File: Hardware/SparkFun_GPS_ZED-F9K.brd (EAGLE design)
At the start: 43.2 x 43.2 mm, 47 parts, among them J1 QWIIC_RIGHT_ANGLE, J4 U.FL, J6 QWIIC_RIGHT_ANGLE, U1 UBLOX_ZED_F9K, U2 3.3V, U3 TRIPLE_BUFFER_74LVC3G07

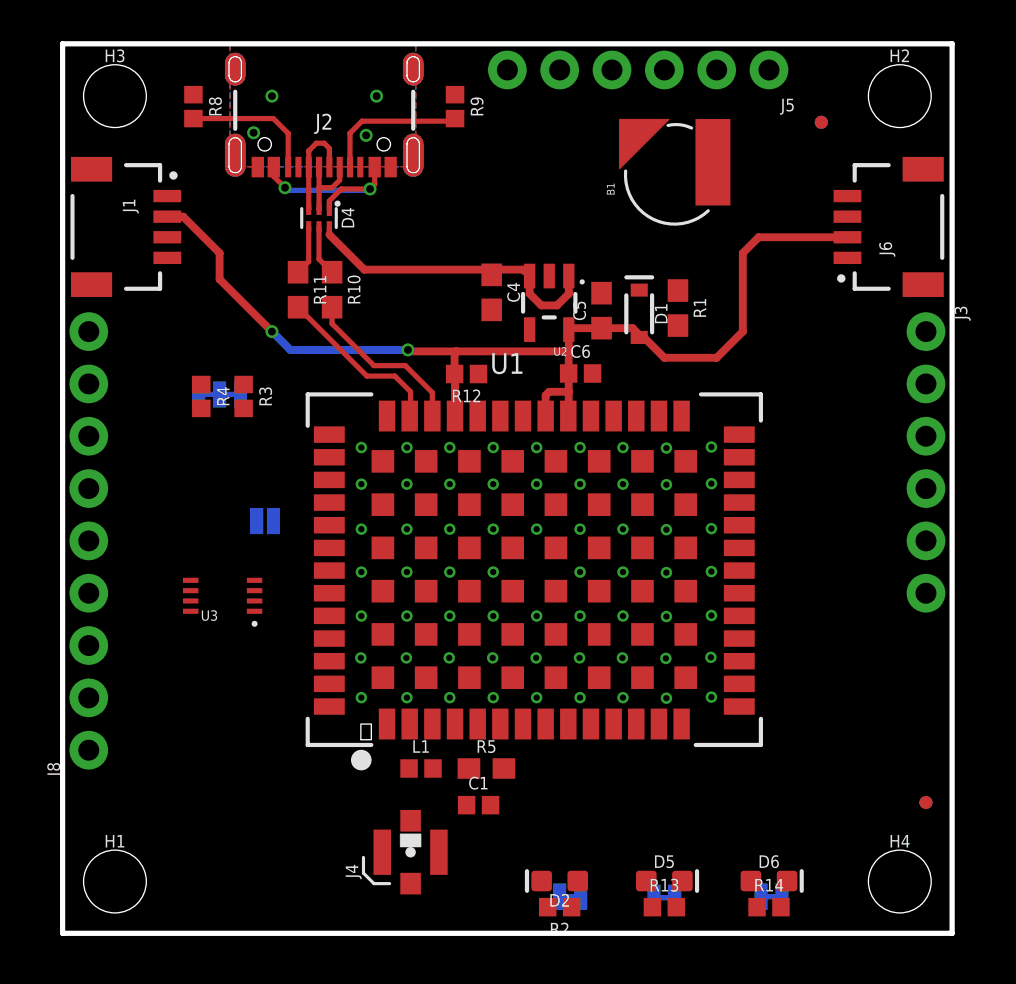
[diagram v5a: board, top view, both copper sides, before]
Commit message: Finalizes trace work for the Breakout board
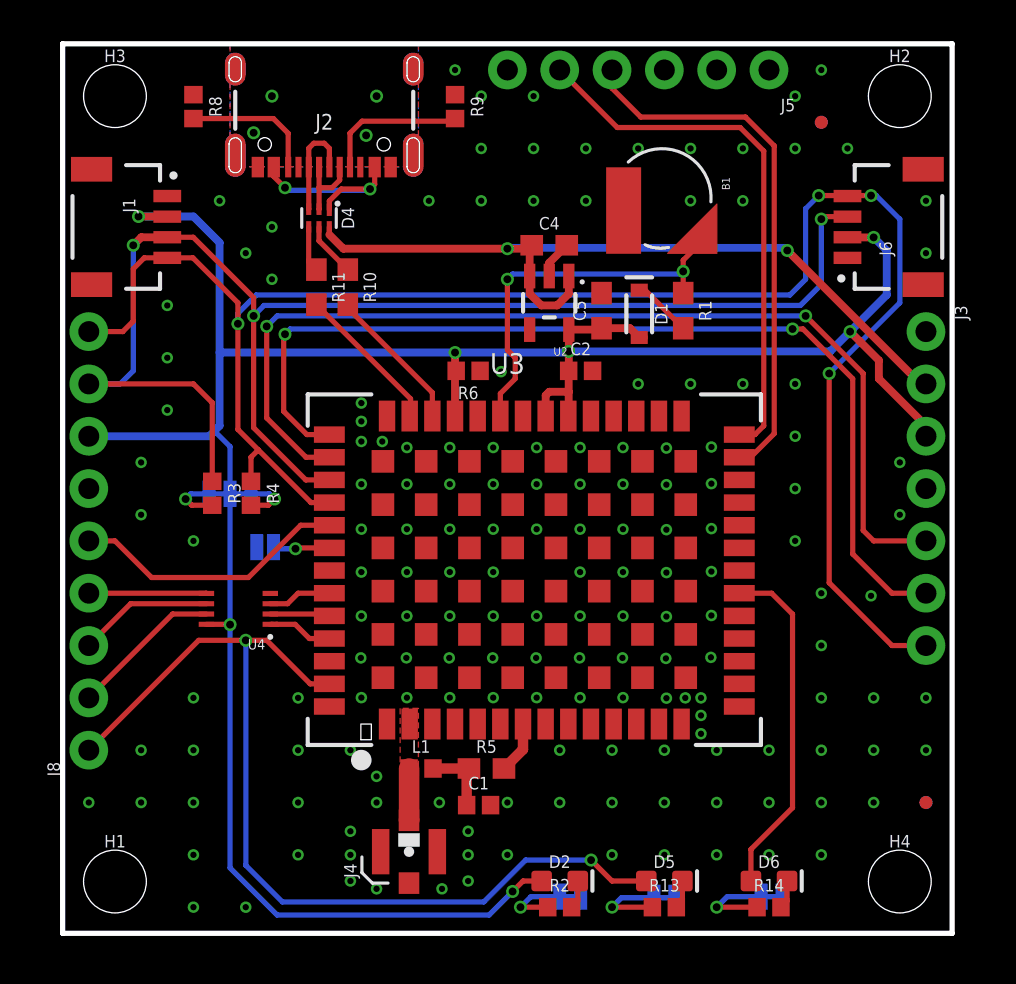
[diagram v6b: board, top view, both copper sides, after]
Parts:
- removed C6: 1.0uF, SparkFun-Capacitors:0402
- removed R12: 100K, SparkFun-Resistors:0402
- removed U1: UBLOX_ZED_F9K, classified:UBLOX_ZED_F9K
- added C2: 1.0uF, SparkFun-Capacitors:0402
- added R6: 100K, SparkFun-Resistors:0402
- added U4: TRIPLE_BUFFER_74LVC3G07, classified:SOP_8-PIN
- J3: device SparkFun-Connectors:1X06_NO_SILK -> SparkFun-Connectors:1X07_NO_SILK
- U3: value TRIPLE_BUFFER_74LVC3G07 -> UBLOX_ZED_F9K; device classified:SOP_8-PIN -> classified:UBLOX_ZED_F9K
- moved U3 15.2 mm to (22.9, 17.8), turned to 0 degrees
- moved R4 5.28 mm to (9.14, 21.4)
- moved R3 4.94 mm to (7.26, 21.4)
- moved JP2 4.85 mm to (8.13, 21.3), turned to 180 degrees
- moved C4 3.61 mm to (23.6, 33.4), turned to 0 degrees
- moved B1 1.31 mm to (29.1, 35.7), turned to 270 degrees
- moved JP1 1.27 mm to (9.83, 18.7)
- moved R11 0.90 mm to (12.3, 31.4)
- moved R10 0.77 mm to (13.8, 31.4)
- moved R1 0.28 mm to (30.1, 30.2)
- moved J4 0.08 mm to (16.8, 3.96)
- turned D2 to 0 degrees
- turned PWR to 0 degrees
- turned R2 to 0 degrees
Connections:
- removed net DIR: U1.P23
- removed net SCK: J3.6
- removed net WT: U1.P22
- net !CS: now also J3.4; no longer J3.3
- net !RESET_IN: now also U3.P49, U4.P3; no longer U1.P49, U3.P1
- net !RESET_OUT: now also U4.P7; no longer U3.P7
- net !SAFEBOOT_IN: now also U4.P6; no longer U1.P50, U3.P6
- net !SAFEBOOT_OUT: now also U3.P50, U4.P2; no longer U3.P2
- net 3.3V: now also C2.1, J3.3, R6.2, U3.P33, U3.P34, U3.P38, U4.P8; no longer C6.1, R12.2, U1.P33, U1.P34, U1.P38, U3.P8
- net DMINUS: now also U3.P39; no longer U1.P39
- net DPLUS: now also U3.P40; no longer U1.P40
- net D_SEL: now also U3.P47; no longer U1.P47
- net GND: now also C2.2, R6.1, U3.G1, U3.G10, U3.G11, U3.G12, U3.G13, U3.G14, U3.G15, U3.G16, U3.G17, U3.G18, U3.G19, U3.G2, U3.G20, U3.G21, U3.G22, U3.G23, U3.G24, U3.G25, U3.G26, U3.G27, U3.G28, U3.G29, U3.G3, U3.G30, U3.G31, U3.G32, U3.G33, U3.G34, U3.G35, U3.G36, U3.G37, U3.G38, U3.G39, U3.G4, U3.G40, U3.G41, U3.G42, U3.G43, U3.G44, U3.G45, U3.G46, U3.G47, U3.G48, U3.G5, U3.G6, U3.G7, U3.G8, U3.G9, U3.P1, U3.P12, U3.P14, U3.P3, U3.P32, U3.P37, U3.P41, U3.P48, U4.P4; no longer C6.2, R12.1, U1.G1, U1.G10, U1.G11, U1.G12, U1.G13, U1.G14, U1.G15, U1.G16, U1.G17, U1.G18, U1.G19, U1.G2, U1.G20, U1.G21, U1.G22, U1.G23, U1.G24, U1.G25, U1.G26, U1.G27, U1.G28, U1.G29, U1.G3, U1.G30, U1.G31, U1.G32, U1.G33, U1.G34, U1.G35, U1.G36, U1.G37, U1.G38, U1.G39, U1.G4, U1.G40, U1.G41, U1.G42, U1.G43, U1.G44, U1.G45, U1.G46, U1.G47, U1.G48, U1.G5, U1.G6, U1.G7, U1.G8, U1.G9, U1.P1, U1.P12, U1.P14, U1.P3, U1.P32, U1.P37, U1.P41, U1.P48, U3.P4
- net INT_IN: now also U3.P51, U4.P1; no longer U1.P51, U3.P3
- net INT_OUT: now also U4.P5; no longer U3.P5
- net PPS: now also U3.P53; no longer U1.P53
- net RF_IN: now also U3.P2; no longer U1.P2
- net RTK_STAT: now also U3.P20; no longer U1.P20
- net RXI/MOSI: now also J3.5, U3.P43; no longer J3.4, U1.P43
- net RXI2: now also U3.P26; no longer U1.P26
- net SCL/CLK: now also J3.7, U3.P45; no longer U1.P45
- net SDA/!CS: now also U3.P44; no longer U1.P44
- net TXO/MISO: now also J3.6, U3.P42; no longer J3.5, U1.P42
- net TXO2: now also U3.P27; no longer U1.P27
- net TX_READY: now also U3.P46; no longer U1.P46
- net V_BATT: now also U3.P36; no longer U1.P36
- net V_RF: now also U3.P7; no longer U1.P7
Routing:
- net SCL/CLK: track 0.00 -> 87.4 mm, vias 0 -> 4
- net SDA/!CS: track 0.00 -> 69.6 mm, vias 0 -> 3
- net 3.3V: track 51.5 -> 119.1 mm, vias 2 -> 7
- net RXI/MOSI: track 0.00 -> 49.5 mm, vias 0 -> 2
- net TXO/MISO: track 0.00 -> 48.0 mm, vias 0 -> 2
- net PPS: track 0.00 -> 47.1 mm, vias 0 -> 2
- net TXO2: track 0.00 -> 26.2 mm
- net RXI2: track 0.00 -> 26.1 mm
- net VIN: track 15.2 -> 39.1 mm, vias 0 -> 2
- net V_BATT: track 0.00 -> 18.8 mm, vias 0 -> 2
- net RTK_STAT: track 0.00 -> 16.8 mm
- net TX_READY: track 0.00 -> 13.5 mm
- net !RESET_OUT: track 0.00 -> 7.40 mm
- net !SAFEBOOT_IN: track 0.00 -> 6.55 mm
- net INT_OUT: track 0.00 -> 5.71 mm
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- added copper zone on layer 1, net RF_IN

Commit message: Adds a few more vias
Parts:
- moved C1 0.25 mm to (20.2, 6.48)
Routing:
- net GND: vias 162 -> 166
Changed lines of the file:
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@@
 <attribute name="REV" value="" x="1.778" y="-16.256" size="1.778" layer="27" font="vector" ratio="15" display="off"/>
 </element>
-<element name="C1" library="SparkFun-Capacitors" package="0402" value="0.1uF" x="20.193" y="6.223" smashed="yes">
-<attribute name="NAME" x="20.193" y="6.985" size="0.6096" layer="25" font="vector" ratio="20" align="bottom-center"/>
-<attribute name="PROD_ID" value="CAP-12416" x="20.193" y="6.223" size="1.778" layer="27" font="vector" ratio="15" display="off"/>
-<attribute name="VALUE" x="20.193" y="5.461" size="0.6096" layer="27" font="vector" ratio="20" align="top-center"/>
+<element name="C1" library="SparkFun-Capacitors" package="0402" value="0.1uF" x="20.193" y="6.477" smashed="yes">
+<attribute name="NAME" x="20.193" y="7.239" size="0.6096" layer="25" font="vector" ratio="20" align="bottom-center"/>
+<attribute name="PROD_ID" value="CAP-12416" x="20.193" y="6.477" size="1.778" layer="27" font="vector" ratio="15" display="off"/>
+<attribute name="VALUE" x="20.193" y="5.715" size="0.6096" layer="27" font="vector" ratio="20" align="top-center"/>
 </element>
 <element name="L1" library="SparkFun-Coils" package="0402" value="3.9NH" x="17.399" y="8.001" smashed="yes">
@@
 <via x="13.97" y="2.54" extent="1-16" drill="0.3048"/>
 <via x="13.97" y="4.953" extent="1-16" drill="0.3048"/>
+<via x="20.32" y="31.75" extent="1-16" drill="0.3048"/>
+<via x="17.78" y="31.75" extent="1-16" drill="0.3048"/>
+<via x="15.24" y="31.75" extent="1-16" drill="0.3048"/>
+<via x="15.24" y="34.29" extent="1-16" drill="0.3048"/>
 </signal>
 <signal name="3.3V">
@@
 <wire x1="19.724" y1="8.001" x2="17.979" y2="8.001" width="0.508" layer="1"/>
 <wire x1="19.724" y1="8.001" x2="19.613" y2="7.89" width="0.508" layer="1"/>
-<wire x1="19.613" y1="7.89" x2="19.613" y2="6.223" width="0.508" layer="1"/>
+<wire x1="19.613" y1="7.89" x2="19.613" y2="6.477" width="0.508" layer="1"/>
 </signal>
 <signal name="V_RF">

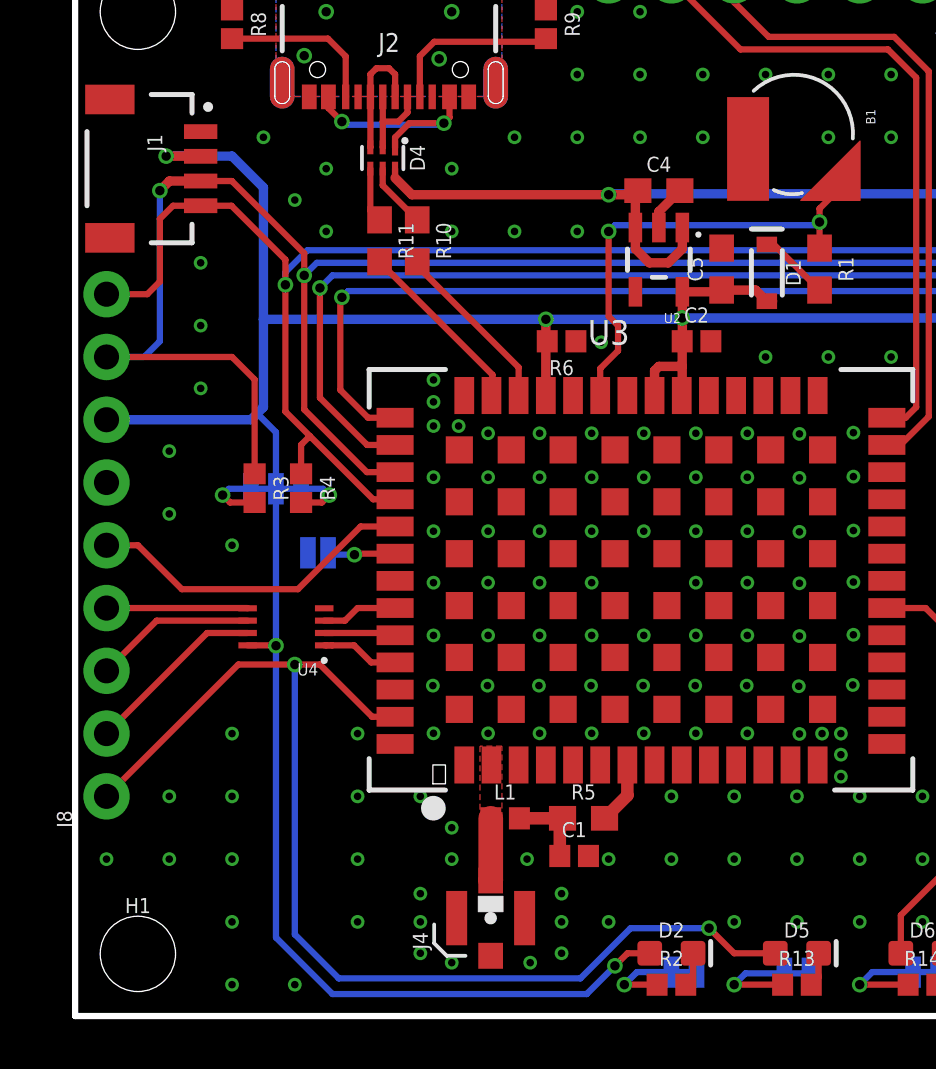
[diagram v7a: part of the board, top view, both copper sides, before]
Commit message: Updates Modules, adjusts ground pour.
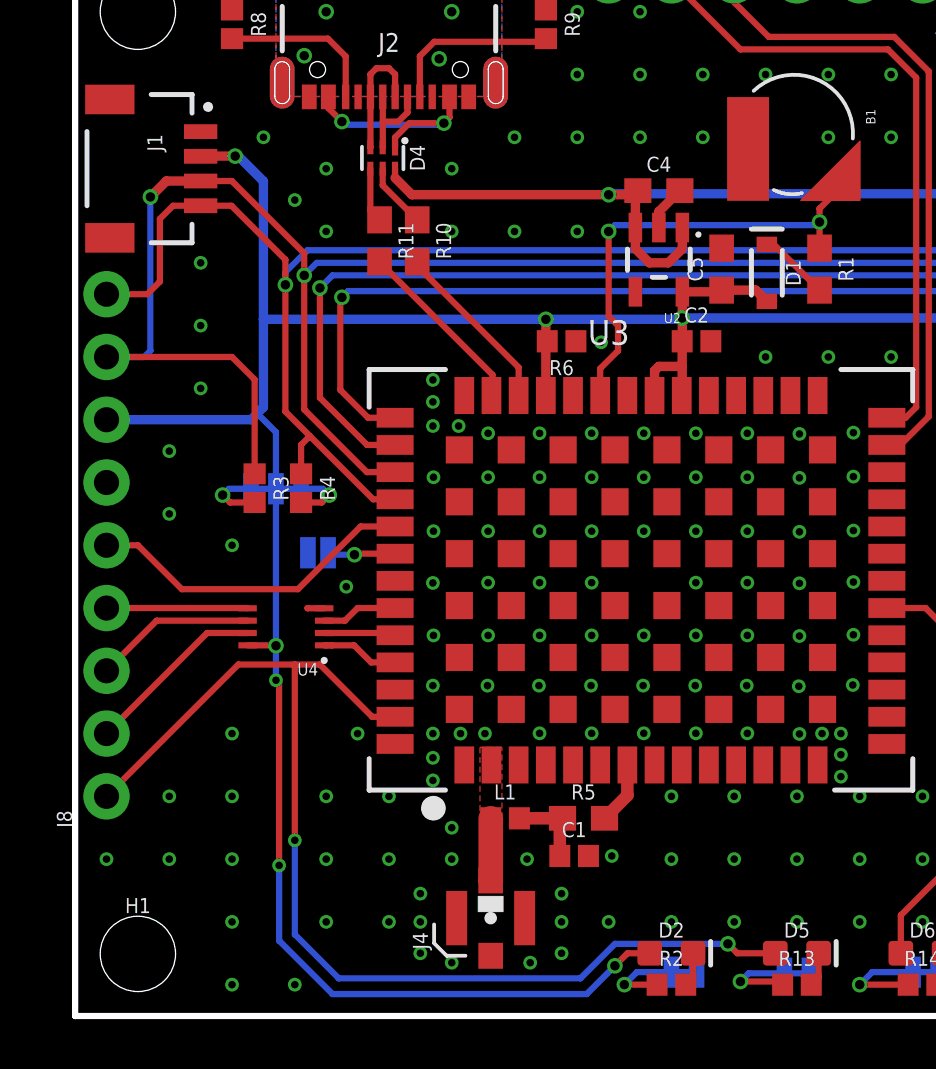
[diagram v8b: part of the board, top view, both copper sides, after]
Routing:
- net 3.3V: track 119.1 -> 116.4 mm, vias 7 -> 9
- net GND: track 1.85 -> 2.53 mm, vias 166 -> 173
- net PPS: track 47.1 -> 46.6 mm
- net N$23: track 4.18 -> 3.67 mm
